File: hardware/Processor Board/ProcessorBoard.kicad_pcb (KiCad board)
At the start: 2 copper layers, 160 x 100 mm, 18 parts, among them IC1 74HC00, IC2 W65C02, IC4 SYSTEM ROM, IC5 RAM, SW1 ~NMI, X1 BUS

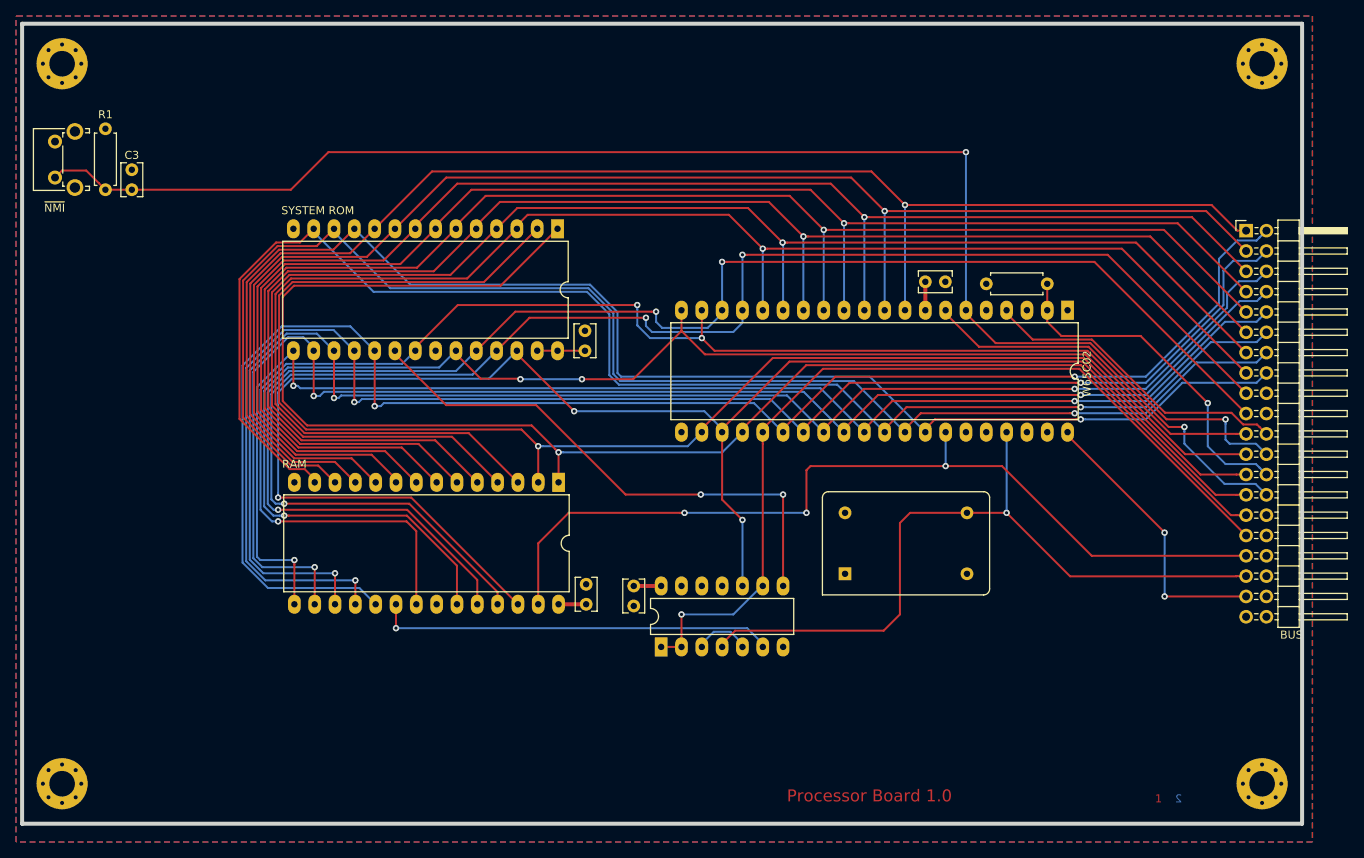
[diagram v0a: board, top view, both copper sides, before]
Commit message: Update processor board routing
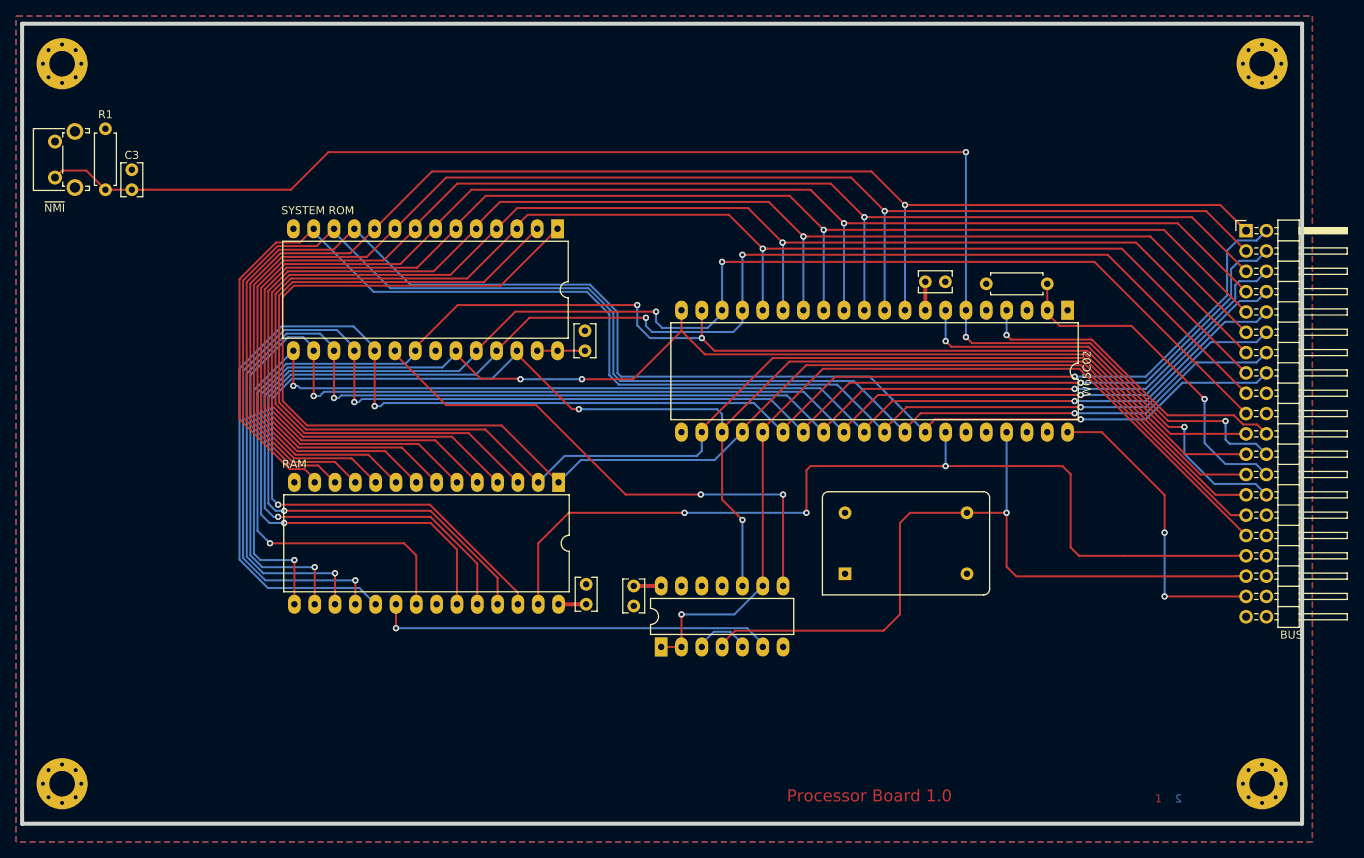
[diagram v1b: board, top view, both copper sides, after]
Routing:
- net /Processor/R~W: track 112.5 -> 117.9 mm
- net /Processor/CLOCK_OSC: track 92.8 -> 96.7 mm
- net /Processor/A13: track 207.6 -> 210.9 mm
- net /Processor/SYNC: track 51.1 -> 53.9 mm, vias 1 -> 2
- net /Processor/A11: track 184.5 -> 187.1 mm
- net /Processor/~RESET: track 35.7 -> 38.2 mm
- net /Processor/A9: track 190.2 -> 192.5 mm
- net /Processor/A8: track 191.4 -> 193.6 mm
- net /Processor/~NMI: track 183.7 -> 185.3 mm, vias 2 -> 3
- net /Processor/~IRQ: track 39.1 -> 40.7 mm, vias 0 -> 1
- net /Processor/A14: track 190.2 -> 189.6 mm, vias 1 -> 0
- net /Processor/A12: track 187.6 -> 188.2 mm, vias 1 -> 0
- net /Processor/RDY: track 43.2 -> 42.7 mm
- net /Processor/D5: track 186.3 -> 186.9 mm
- net /Processor/D7: track 197.2 -> 197.8 mm
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
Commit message: Update processor board
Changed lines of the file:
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@@
     (add_net "Net-(IC1-Pad6)")
     (add_net "Net-(IC1-Pad8)")
+    (add_net "Net-(IC2-Pad1)")
+    (add_net "Net-(IC2-Pad3)")
+    (add_net "Net-(IC2-Pad35)")
+    (add_net "Net-(IC2-Pad39)")
+    (add_net "Net-(IC2-Pad5)")
+    (add_net "Net-(X1-Pad18)")
+    (add_net "Net-(X1-Pad20)")
+    (add_net "Net-(X1-Pad30)")
+    (add_net "Net-(X1-Pad32)")
+    (add_net "Net-(X1-Pad34)")
+    (add_net "Net-(X1-Pad36)")
+    (add_net "Net-(X1-Pad38)")
+    (add_net "Net-(XTAL1-Pad1)")
   )
   (net_class Power ""
@@
       (effects (font (size 1 1) (thickness 0.15)))
     )
-    (fp_text value BUS (at 5.655 50.53) (layer F.SilkS)
+    (fp_text value BUS (at 1.178 -2.832) (layer F.SilkS)
       (effects (font (size 1 1) (thickness 0.15)))
     )

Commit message: Rename NMI push button
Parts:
- SW1: value ~NMI -> NMI
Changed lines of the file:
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@@
       (effects (font (size 1 1) (thickness 0.15)))
     )
-    (fp_text value ~NMI (at -3.81 -0.05 180) (layer F.SilkS)
+    (fp_text value NMI (at -3.81 -0.05 180) (layer F.SilkS)
       (effects (font (size 1 1) (thickness 0.15)))
     )

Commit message: Working on hardware
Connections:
- net /Processor/CLOCK_OSC renamed /Processor/CLOCK
- X1 pad 18: (no net) -> /Processor/~IRQ
- X1 pad 20: (no net) -> /Processor/RDY
- X1 pad 22: /Processor/~IRQ -> /Processor/~NMI
- X1 pad 24: /Processor/~NMI -> /Processor/SYNC
- X1 pad 26: /Processor/RDY -> (no net)
- X1 pad 28: /Processor/SYNC -> (no net)
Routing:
- net /Processor/RDY: track 42.7 -> 37.3 mm
- net /Processor/SYNC: track 53.9 -> 50.8 mm
- net /Processor/~NMI: track 185.3 -> 183.9 mm
- net /Processor/~IRQ: track 40.7 -> 39.7 mm, vias 1 -> 2
- net /Processor/A11: vias 3 -> 4
- net /Processor/A10: vias 3 -> 4
